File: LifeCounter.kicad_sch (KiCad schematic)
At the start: 36 parts, among them IC1 STM32H562RGT6, IC2 AP3012KTR-E1, IC3 MCP73831T-2ATI_OT, IC4 AP2112K-3.3TRG1, J1 54104-4531, J2 USB_C_Receptacle_USB2.0_14P

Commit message: FIX: added missing GND on lcd backlight driver
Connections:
- net GND: now also C1.2, C2.2, C3.2, IC2.2 (GND), R1.2
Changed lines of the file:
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@@
 	(paper "A4")
 	(junction
-		(at 50.8 71.12)
+		(at 200.66 132.08)
 		(diameter 0)
 		(color 0 0 0 0)
 	)
 	(junction
-		(at 200.66 132.08)
+		(at 50.8 71.12)
 		(diameter 0)
 		(color 0 0 0 0)
@@
 	(wire
 		(pts
+			(xy 200.66 132.08) (xy 205.74 132.08)
+		)
+		(stroke
+			(width 0)
+			(type default)
+		)
+	)
+	(wire
+		(pts
 			(xy 205.74 129.54) (xy 205.74 132.08)
 		)
@@
 	(wire
 		(pts
-			(xy 118.11 62.23) (xy 129.54 62.23)
+			(xy 200.66 135.89) (xy 200.66 132.08)
 		)
 		(stroke
@@
 	(wire
 		(pts
-			(xy 120.65 76.2) (xy 129.54 76.2)
+			(xy 118.11 62.23) (xy 129.54 62.23)
 		)
 		(stroke
@@
 	(wire
 		(pts
-			(xy 87.63 116.84) (xy 87.63 109.22)
+			(xy 120.65 76.2) (xy 129.54 76.2)
 		)
 		(stroke
@@
 	(wire
 		(pts
-			(xy 55.88 59.69) (xy 50.8 59.69)
+			(xy 87.63 116.84) (xy 87.63 109.22)
 		)
 		(stroke
@@
 	(wire
 		(pts
-			(xy 86.36 86.36) (xy 71.12 86.36)
+			(xy 55.88 59.69) (xy 50.8 59.69)
 		)
 		(stroke
@@
 	(wire
 		(pts
-			(xy 54.61 22.86) (xy 46.99 22.86)
+			(xy 86.36 86.36) (xy 71.12 86.36)
 		)
 		(stroke
@@
 	(wire
 		(pts
-			(xy 196.85 114.3) (xy 201.93 114.3)
+			(xy 54.61 22.86) (xy 46.99 22.86)
 		)
 		(stroke
@@
 	(wire
 		(pts
-			(xy 80.01 26.67) (xy 86.36 26.67)
+			(xy 196.85 114.3) (xy 201.93 114.3)
 		)
 		(stroke
@@
 	(wire
 		(pts
-			(xy 200.66 132.08) (xy 161.29 132.08)
+			(xy 80.01 26.67) (xy 86.36 26.67)
 		)
 		(stroke
@@
 	(wire
 		(pts
-			(xy 205.74 132.08) (xy 200.66 132.08)
-		)
-		(stroke
-			(width 0)
-			(type default)
-		)
-	)
-	(wire
-		(pts
 			(xy 226.06 101.6) (xy 226.06 109.22)
 		)
@@
 	(wire
 		(pts
+			(xy 161.29 132.08) (xy 200.66 132.08)
+		)
+		(stroke
+			(width 0)
+			(type default)
+		)
+	)
+	(wire
+		(pts
 			(xy 82.55 71.12) (xy 82.55 59.69)
 		)
@@
 					(unit 1)
 				)
+			)
+		)
+	)
+	(symbol
+		(lib_id "power:GND")
+		(at 200.66 135.89 0)
+		(unit 1)
+		(exclude_from_sim no)
+		(in_bom yes)
+		(on_board yes)
+		(dnp no)
+		(fields_autoplaced yes)
+		(property "Reference" "#PWR028"
+			(at 200.66 142.24 0)
+			(effects
+				(font
+					(size 1.27 1.27)
+				)
+				(hide yes)
+			)
+		)
+		(property "Value" "GND"
+			(at 200.66 140.97 0)
+			(effects
+				(font
+					(size 1.27 1.27)
+				)
+			)
+		)
+		(property "Footprint" ""
+			(at 200.66 135.89 0)
+			(effects
+				(font
+					(size 1.27 1.27)
+				)
+				(hide yes)
+			)
+		)
+		(property "Datasheet" ""
+			(at 200.66 135.89 0)
+			(effects
+				(font
+					(size 1.27 1.27)
+				)
+				(hide yes)
+			)
+		)
+		(property "Description" "Power symbol creates a global label with name \"GND\" , ground"
+			(at 200.66 135.89 0)
+			(effects
+				(font
+					(size 1.27 1.27)
+				)
+				(hide yes)
+			)
+		)
+		(pin "1"
+		)
+		(instances
+			(project "LifeCounter"
+				(path "/4fcff061-b5b1-4f40-9b81-6bf0aa8b3dad"
+					(reference "#PWR028")
+					(unit 1)
+				)

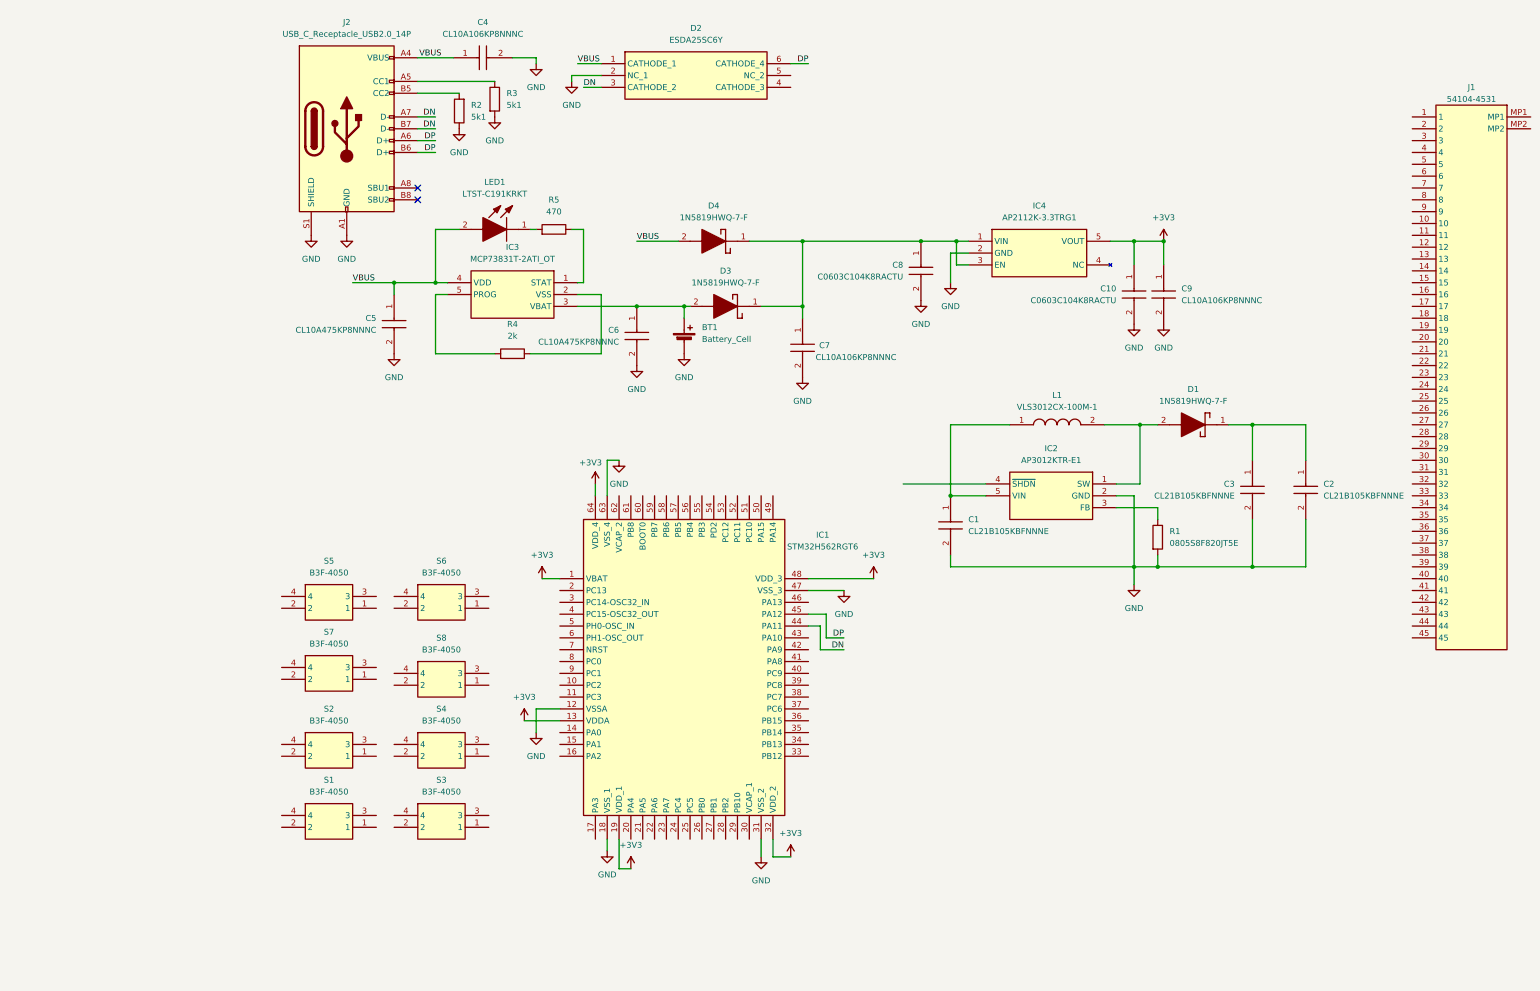
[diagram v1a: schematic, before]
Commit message: capacitor changes
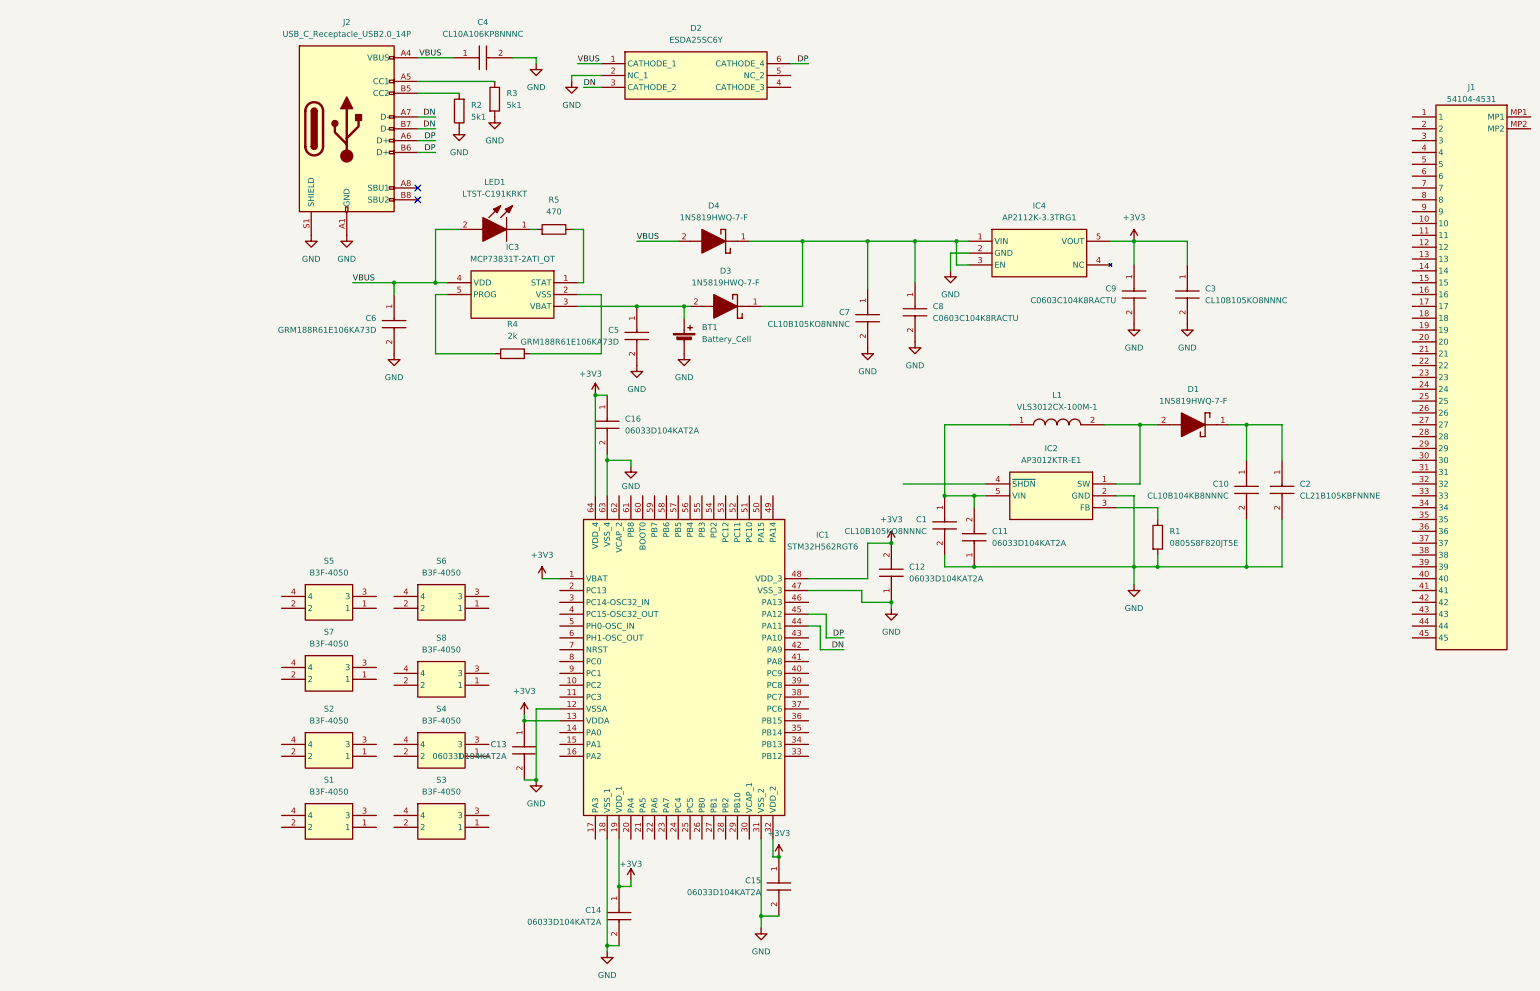
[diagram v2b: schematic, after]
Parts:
- removed C1, C3: CL21B105KBFNNNE, LifeCounter-Footprints:Samsung_CAPC2012X135M, symbol LifeCounter-Symbols:CL21B105KBFNNNE
- removed C10: C0603C104K8RACTU, LifeCounter-Footprints:Kemet_C0603, symbol LifeCounter-Symbols:C0603C104K8RACTU
- removed C5, C6: CL10A475KP8NNNC, LifeCounter-Footprints:Samsung_CAPC1608X90M, symbol LifeCounter-Symbols:CL10A475KP8NNNC
- removed C7, C9: CL10A106KP8NNNC, LifeCounter-Footprints:Samsung_CAPC1608X90M, symbol LifeCounter-Symbols:CL10A106KP8NNNC
- added C1, C3, C7: CL10B105KO8NNNC, LifeCounter-Footprints:Samsung_CAPC1608X90M, symbol LifeCounter-Symbols:CL10B105KO8NNNC
- added C10: CL10B104KB8NNNC, LifeCounter-Footprints:Samsung_CAPC1608X90M, symbol LifeCounter-Symbols:CL10B104KB8NNNC
- added C11, C12, C13, C14, C15, C16: 06033D104KAT2A, LifeCounter-Footprints:Kyocera_CAPC1608X90M, symbol LifeCounter-Symbols:06033D104KAT2A
- added C5, C6: GRM188R61E106KA73D, LifeCounter-Footprints:Murata_GRM18x, symbol LifeCounter-Symbols:GRM188R61E106KA73D
- added C9: C0603C104K8RACTU, LifeCounter-Footprints:Kemet_C0603, symbol LifeCounter-Symbols:C0603C104K8RACTU
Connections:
- net +3V3: now also C12.2, C13.1, C14.1, C15.1, C16.1, C3.1, C9.1
- net GND: now also C1.2, C10.2, C11.1, C12.1, C13.2, C14.2, C15.2, C16.2, C3.2, C5.2, C6.2, C7.2, C9.2
- net VBUS: now also C6.1
- net at C2.1, D1.1 (K): now also C10.1
- net at C8.1, D3.1 (K), D4.1 (K)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: now also C7.1
- net at BT1.1 (+), D3.2 (A), IC3.3 (VBAT): now also C5.1
- net at IC2.5 (VIN), L1.1: now also C1.1, C11.2
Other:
- moved on the sheet: C2, C8

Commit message: divided schematic into two sheets
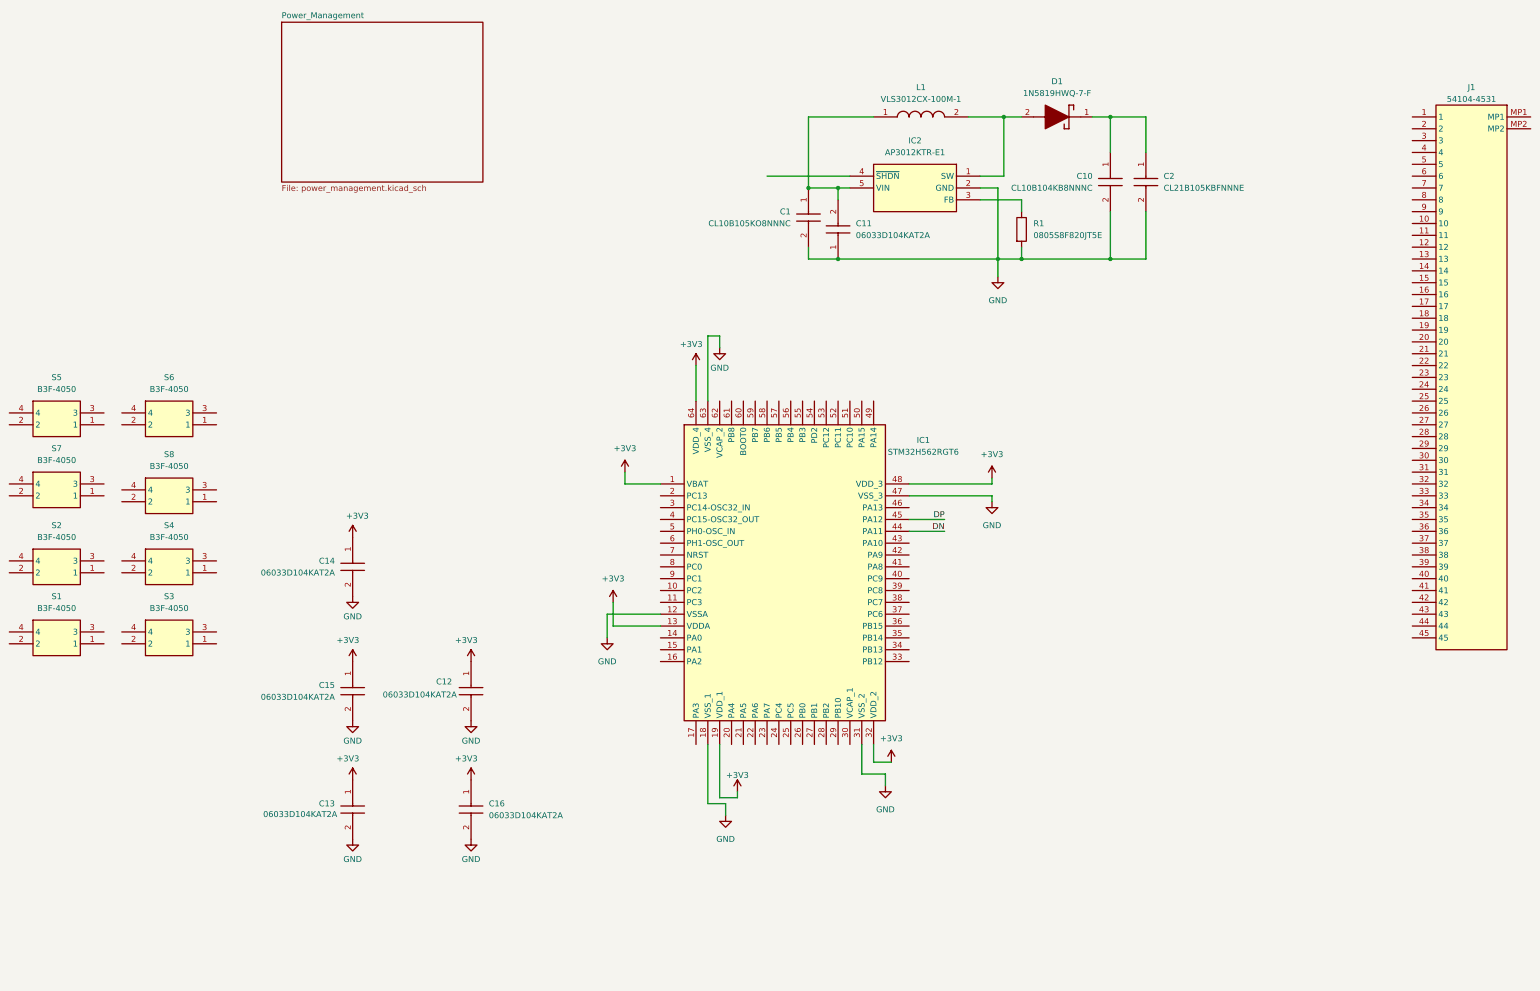
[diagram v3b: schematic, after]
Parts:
- removed BT1: Battery_Cell, symbol Device:Battery_Cell
- removed C3, C7: CL10B105KO8NNNC, LifeCounter-Footprints:Samsung_CAPC1608X90M, symbol LifeCounter-Symbols:CL10B105KO8NNNC
- removed C4: CL10A106KP8NNNC, LifeCounter-Footprints:Samsung_CAPC1608X90M, symbol LifeCounter-Symbols:CL10A106KP8NNNC
- removed C5, C6: GRM188R61E106KA73D, LifeCounter-Footprints:Murata_GRM18x, symbol LifeCounter-Symbols:GRM188R61E106KA73D
- removed C8, C9: C0603C104K8RACTU, LifeCounter-Footprints:Kemet_C0603, symbol LifeCounter-Symbols:C0603C104K8RACTU
- removed D2: ESDA25SC6Y, LifeCounter-Footprints:STMicroelectronics_SOT95P280X145-6M, symbol LifeCounter-Symbols:ESDA25SC6Y
- removed D3, D4: 1N5819HWQ-7-F, LifeCounter-Footprints:Diodes-Inc_SOD3716X145M, symbol LifeCounter-Symbols:1N5819HWQ-7-F
- removed IC3: MCP73831T-2ATI_OT, LifeCounter-Footprints:Microchip_SOT95P270X145-5M, symbol LifeCounter-Symbols:MCP73831T-2ATI_OT
- removed IC4: AP2112K-3.3TRG1, LifeCounter-Footprints:Diodes_Inc-SOT95P285X140-5M, symbol LifeCounter-Symbols:AP2112K-3.3TRG1
- removed J2: USB_C_Receptacle_USB2.0_14P, Connector_USB:USB_C_Receptacle_GCT_USB4105-xx-A_16P_TopMnt_Horizontal, symbol Connector:USB_C_Receptacle_USB2.0_16P
- removed LED1: LTST-C191KRKT, LifeCounter-Footprints:Liteon_LEDC1608X55M, symbol LifeCounter-Symbols:LTST-C191KRKT
- removed R2, R3: 5k1, Resistor_SMD:R_0603_1608Metric_Pad0.98x0.95mm_HandSolder, symbol Device:R
- removed R4: 2k, Resistor_SMD:R_0603_1608Metric_Pad0.98x0.95mm_HandSolder, symbol Device:R
- removed R5: 470, Resistor_SMD:R_0603_1608Metric_Pad0.98x0.95mm_HandSolder, symbol Device:R
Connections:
- net +3V3: now also C12.1; no longer C12.2
- net GND: now also C12.2; no longer C12.1
- no-connect marks 2 -> 0
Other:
- added sheet Power_Management (power_management.kicad_sch)
- moved on the sheet: C1, C10, C11, C12, C13, C14, C15, C16, C2, D1, IC1, IC2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

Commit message: cleaned up and annotated the schematic
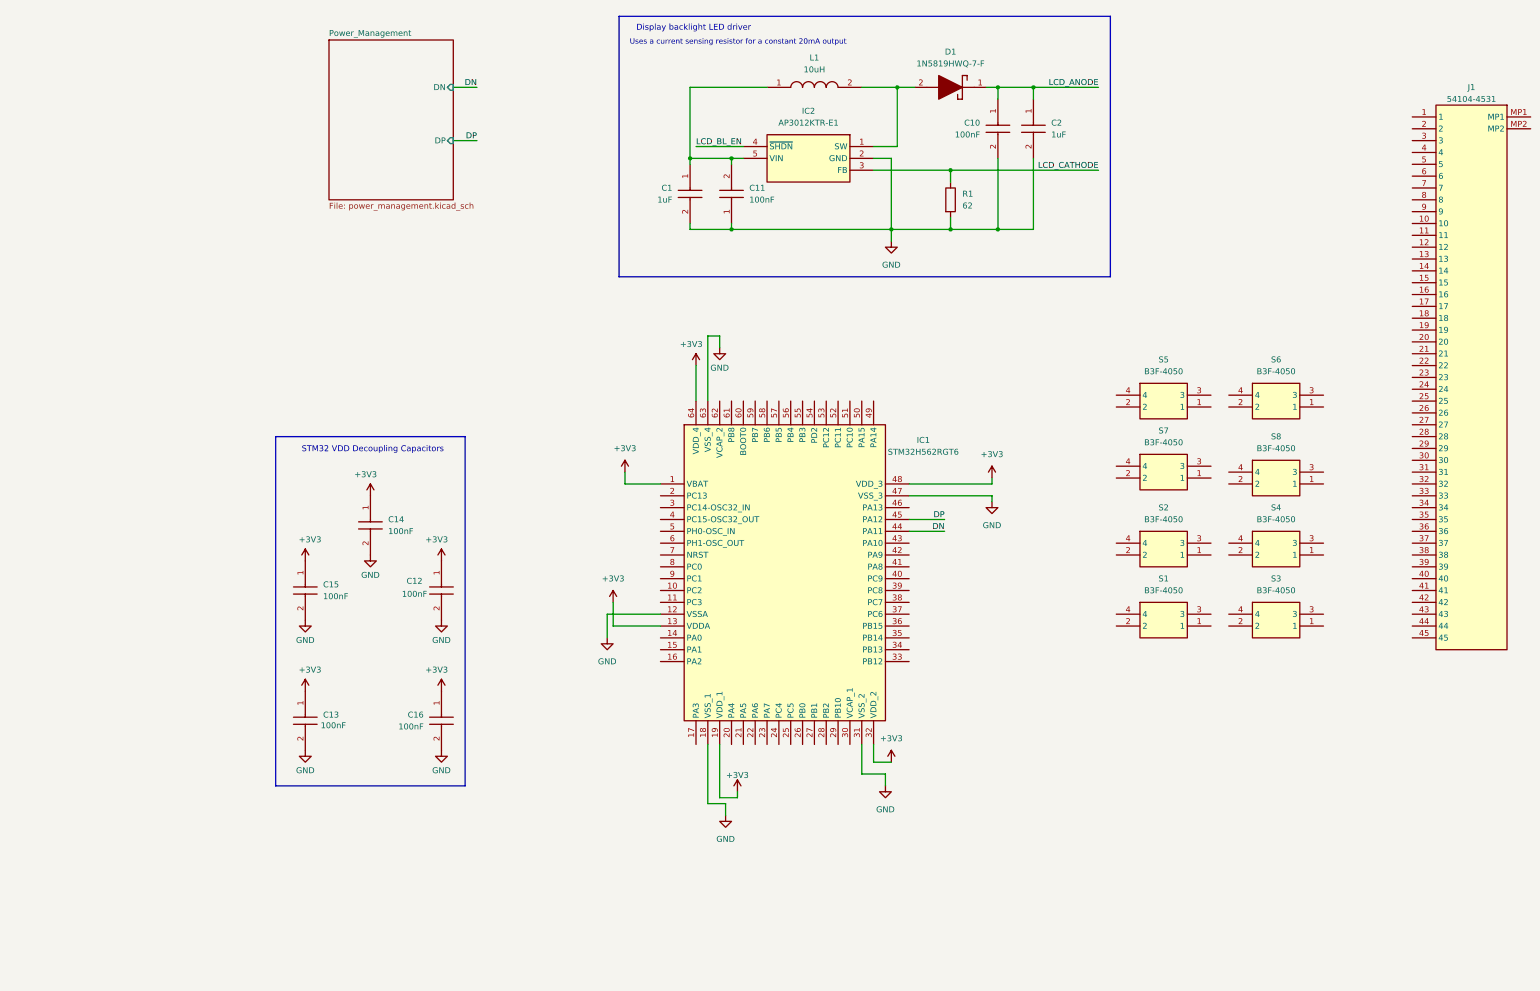
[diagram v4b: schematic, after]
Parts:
- C1: value CL10B105KO8NNNC -> 1uF
- C10: value CL10B104KB8NNNC -> 100nF
- C11, C12, C13, C14, C15, C16: value 06033D104KAT2A -> 100nF
- C2: value CL21B105KBFNNNE -> 1uF
- L1: value VLS3012CX-100M-1 -> 10uH
- R1: value 0805S8F820JT5E -> 62
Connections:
- net LCD_ANODE: now reaches C10.1, C2.1, D1.1 (K)
- net LCD_CATHODE: now reaches IC2.3 (FB), R1.1
- net LCD_BL_EN: now reaches IC2.4 (~{SHDN})
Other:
- sheet Power_Management ports: added DN, DP; removed none
- note added: "Display backlight LED driver"
- note added: "STM32 VDD Decoupling Capacitors"
- note added: "Uses a current sensing resistor for a constant 20mA output"
- moved on the sheet: C1, C10, C11, C12, C13, C14, C15, C16, C2, D1, IC2, L1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
